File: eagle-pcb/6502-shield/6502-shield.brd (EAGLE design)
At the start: 101.6 x 53.3 mm, 45 parts, among them SW1 MCSLPT4644B1TR-TACT-SW, SW2 PCM12SMTR-SPDT-RIGHT-ANG, SW3 MCSLPT4644B1TR-TACT-SW, U1 AT28C256TSOP-28, U2 W65C02S, U3 AS6C62256, U4 W65C22, U5 MACHXO-FPGA100TQFP

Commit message: fully routed, getting close
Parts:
- removed D10, D8, D9: ACDC02-41SGWA-DUAL-7SEG, 6502-shield:ACDC02-41S-DUAL-7SEG
- removed R10, R11, R12, R13, R14, R15, R16, R17: 330, rcl:R0402
- removed SW1: MCSLPT4644B1TR-TACT-SW, 6502-shield:MCSLPT4644B1TR-TACT-SW
- removed U$1: CRYSTAL-OSC-DIP8/4, 6502-shield:DIP8/4
- removed U1: AT28C256TSOP-28, 6502-shield:SOP55P1340X120-28N
- removed U2: W65C02S, 6502-shield:QFP80P1200X1200X160-44N
- removed U3: AS6C62256, 6502-shield:SOP55P1340X120-28N
- removed U4: W65C22, 6502-shield:QFP80P1200X1200X160-44N
- added C1, C2, C5, C6, C7: 0.1uF, rcl:C0402
- added CPU: W65C02S, 6502-shield:QFP80P1200X1200X160-44N
- added EEPROM: AT28C256TSOP-28, 6502-shield:SOP55P1340X120-28N
- added EXT_XO: CRYSTAL-OSC-DIP8/4, 6502-shield:DIP8/4
- added PB_RESET: MCSLPT4644B1TR-TACT-SW, 6502-shield:MCSLPT4644B1TR-TACT-SW
- added PIO: W65C22, 6502-shield:QFP80P1200X1200X160-44N
- added RAM: AS6C62256, 6502-shield:SOP55P1340X120-28N
- D1, D2, D3, D4, D5, D6, D7: value (none) -> RED
- moved R18 40.3 mm to (68.9, 8.25), turned to 270 degrees
- moved JP2 35.0 mm to (77.3, 46.3), turned to 180 degrees
- moved C4 27.6 mm to (2.90, 30.1), turned to 180 degrees
- moved JP3 18.8 mm to (78.7, 8.40), turned to 0 degrees
- moved R1 16.8 mm to (20.0, 14.7), turned to 270 degrees
- moved D4 11.9 mm to (10.0, 43.4), turned to 180 degrees
- moved R3 11.3 mm to (12.3, 13.2), turned to 90 degrees
- moved D3 10.1 mm to (10.1, 45.0), turned to 180 degrees
- moved R19 9.32 mm to (72.5, 6.70), turned to 180 degrees
- moved D2 8.73 mm to (10.1, 46.5), turned to 180 degrees
- moved R2 8.51 mm to (15.3, 47.0)
- moved D5 7.74 mm to (20.4, 48.2), turned to 0 degrees
- moved D1 7.67 mm to (10.1, 48.0), turned to 180 degrees
- moved D6 5.72 mm to (20.4, 46.6), turned to 0 degrees
- moved R7 5.01 mm to (15.3, 45.9), turned to 180 degrees
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- renumbered SJ1 to J1, SW2 to SW_RUNHALT, SW3 to PB_STEP, U5 to FPGA
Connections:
- removed net DIGIT1_EN: D8.18, D8.3, FPGA.87
- removed net DIGIT2_EN: D8.13, D8.8, FPGA.89
- removed net DIGIT3_EN: D9.18, D9.3, FPGA.91
- removed net DIGIT4_EN: D9.13, D9.8, FPGA.94
- removed net DIGIT5_EN: D10.18, D10.3, FPGA.95
- removed net DIGIT6_EN: D10.13, D10.8, FPGA.96
- removed net DIGIT_A: FPGA.78, R10.2
- removed net DIGIT_B: FPGA.79, R11.2
- removed net DIGIT_C: FPGA.80, R12.2
- removed net DIGIT_D: FPGA.81, R13.2
- removed net DIGIT_DP: FPGA.86, R17.2
- removed net DIGIT_E: FPGA.82, R14.2
- removed net DIGIT_F: FPGA.83, R15.2
- removed net DIGIT_G: FPGA.85, R16.2
- removed net N$23: D10.12, D10.17, D8.12, D8.17, D9.12, D9.17, R10.1
- removed net N$24: D10.11, D10.16, D8.11, D8.16, D9.11, D9.16, R11.1
- removed net N$25: D10.4, D10.9, D8.4, D8.9, D9.4, D9.9, R12.1
- removed net N$26: D10.2, D10.7, D8.2, D8.7, D9.2, D9.7, R13.1
- removed net N$27: D10.1, D10.6, D8.1, D8.6, D9.1, D9.6, R14.1
- removed net N$28: D10.14, D10.19, D8.14, D8.19, D9.14, D9.19, R15.1
- removed net N$29: D10.15, D10.20, D8.15, D8.20, D9.15, D9.20, R16.1
- removed net N$30: D10.10, D10.5, D8.10, D8.5, D9.10, D9.5, R17.1
- removed net ROM_PGM: FPGA.34, PCB1.45
- new net EEPROM_PGM: FPGA.34, PCB1.23
- net A0: now also CPU.4, EEPROM.17, PCB1.44, PIO.36, RAM.17; no longer PCB1.22, U1.17, U2.4, U3.17, U4.36
- net A1: now also CPU.5, EEPROM.16, PCB1.45, PIO.35, RAM.16; no longer PCB1.24, U1.16, U2.5, U3.16, U4.35
- net A10: now also CPU.15, EEPROM.28, PCB1.34, RAM.28; no longer PCB1.42, U1.28, U2.15, U3.28
- net A11: now also CPU.16, EEPROM.2, PCB1.35, RAM.2; no longer PCB1.44, U1.2, U2.16, U3.2
- net A12: now also CPU.19, EEPROM.9, PCB1.32, RAM.9; no longer PCB1.46, U1.9, U2.19, U3.9
- net A13: now also CPU.20, EEPROM.5, PCB1.33, RAM.5; no longer PCB1.48, U1.5, U2.20, U3.5
- net A14: now also CPU.21, EEPROM.8, PCB1.30, RAM.8; no longer PCB1.50, U1.8, U2.21, U3.8
- net A15: now also CPU.22, PCB1.31; no longer PCB1.52, U2.22
- net A2: now also CPU.7, EEPROM.15, PCB1.42, PIO.34, RAM.15; no longer PCB1.26, U1.15, U2.7, U3.15, U4.34
- net A3: now also CPU.8, EEPROM.14, PCB1.43, PIO.33, RAM.14; no longer PCB1.28, U1.14, U2.8, U3.14, U4.33
- net A4: now also CPU.9, EEPROM.13, PCB1.40, RAM.13; no longer PCB1.30, U1.13, U2.9, U3.13
- net A5: now also CPU.10, EEPROM.12, PCB1.41, RAM.12; no longer PCB1.32, U1.12, U2.10, U3.12
- net A6: now also CPU.11, EEPROM.11, PCB1.38, RAM.11; no longer PCB1.34, U1.11, U2.11, U3.11
- net A7: now also CPU.12, EEPROM.10, PCB1.39, RAM.10; no longer PCB1.36, U1.10, U2.12, U3.10
- net A8: now also CPU.13, EEPROM.4, PCB1.36, RAM.4; no longer PCB1.38, U1.4, U2.13, U3.4
- net A9: now also CPU.14, EEPROM.3, PCB1.37, RAM.3; no longer PCB1.40, U1.3, U2.14, U3.3
- net BE: now also CPU.34; no longer U2.34
- net CLK: now also CPU.35, PCB1.27, PIO.21; no longer PCB1.43, U2.35, U4.21
- net D0: now also CPU.30, EEPROM.18, PCB1.52, PIO.30, RAM.18; no longer PCB1.23, U1.18, U2.30, U3.18, U4.30
- net D1: now also CPU.29, EEPROM.19, PCB1.53, PIO.29, RAM.19; no longer PCB1.25, U1.19, U2.29, U3.19, U4.29
- net D2: now also CPU.28, EEPROM.20, PCB1.50, PIO.28, RAM.20; no longer PCB1.27, U1.20, U2.28, U3.20, U4.28
- net D3: now also CPU.27, EEPROM.22, PCB1.51, PIO.26, RAM.22; no longer PCB1.29, U1.22, U2.27, U3.22, U4.26
- net D4: now also CPU.26, EEPROM.23, PCB1.48, PIO.25, RAM.23; no longer PCB1.31, U1.23, U2.26, U3.23, U4.25
- net D5: now also CPU.25, EEPROM.24, PCB1.49, PIO.24, RAM.24; no longer PCB1.33, U1.24, U2.25, U3.24, U4.24
- net D6: now also CPU.24, EEPROM.25, PCB1.46, PIO.23, RAM.25; no longer PCB1.35, U1.25, U2.24, U3.25, U4.23
- net D7: now also CPU.23, EEPROM.26, PCB1.47, PIO.22, RAM.26; no longer PCB1.37, U1.26, U2.23, U3.26, U4.22
- net DMA: now also PCB1.22; no longer PCB1.47
- net GND: now also C1.2, C2.2, C5.2, C6.2, C7.2, EEPROM.21, EXT_XO.4, PB_RESET.T2, PIO.39, RAM.21; no longer SW1.T2, U$1.4, U1.21, U3.21, U4.39
- net IO_EN: now also PIO.19; no longer U4.19
- net IRQN: now also CPU.43, PIO.17; no longer U2.43, U4.17
- net N$3: now also PB_RESET.T4; no longer SW1.T4
- net N$31: now also CPU.41; no longer U2.41
- net N$34: now also EXT_XO.5; no longer U$1.5
- net OE: now also EEPROM.1, PCB1.25, RAM.1; no longer PCB1.39, U1.1, U3.1
- net PA0: now also PIO.40; no longer U4.40
- net PA1: now also PIO.41; no longer U4.41
- net PA2: now also PIO.42; no longer U4.42
- net PA3: now also PIO.43; no longer U4.43
- net PA4: now also PIO.44; no longer U4.44
- net PA5: now also PIO.1; no longer U4.1
- net PA6: now also PIO.2; no longer U4.2
- net PA7: now also PIO.3; no longer U4.3
- net PB0: now also PIO.4; no longer U4.4
- net PB1: now also PIO.6; no longer U4.6
- net PB2: now also PIO.7; no longer U4.7
- net PB3: now also PIO.8; no longer U4.8
- net PB4: now also PIO.9; no longer U4.9
- net PB5: now also PIO.10; no longer U4.10
- net PB6: now also PIO.11; no longer U4.11
- net PB7: now also PIO.12; no longer U4.12
- net RAM_EN: now also RAM.27; no longer U3.27
- net RESETN: now also CPU.38, PIO.31; no longer U2.38, U4.31
- net ROM_EN: now also EEPROM.27; no longer U1.27
- net RW: now also CPU.32, PIO.18; no longer U2.32, U4.18
- net VCC: now also C1.1, C2.1, C5.1, C6.1, C7.1, CPU.1, CPU.3, CPU.31, EEPROM.7, EXT_XO.8, PIO.15, PIO.20, RAM.7; no longer U$1.8, U1.7, U2.1, U2.3, U2.31, U3.7, U4.15, U4.20
- net WE: now also EEPROM.6, PCB1.29, RAM.6; no longer PCB1.41, U1.6, U3.6
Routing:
- net VCC: track 0.00 -> 368.6 mm, vias 0 -> 8
- net IRQN: track 0.00 -> 178.4 mm, vias 0 -> 4
- net CLK: track 0.00 -> 159.1 mm, vias 0 -> 4
- net EEPROM_PGM: track 0.00 -> 153.0 mm, vias 0 -> 2
- net DMA: track 0.00 -> 137.7 mm, vias 0 -> 2
- net RW: track 0.00 -> 132.3 mm, vias 0 -> 3
- net A10: track 0.00 -> 123.9 mm, vias 0 -> 4
- net D0: track 0.00 -> 123.1 mm, vias 0 -> 5
- net D1: track 0.00 -> 118.4 mm, vias 0 -> 5
- net A13: track 0.00 -> 117.3 mm, vias 0 -> 4
- net WE: track 0.00 -> 114.5 mm, vias 0 -> 3
- net D2: track 0.00 -> 112.4 mm, vias 0 -> 5
- net A3: track 0.00 -> 111.1 mm, vias 0 -> 5
- net A14: track 0.00 -> 108.8 mm, vias 0 -> 4
- net A15: track 0.00 -> 108.2 mm, vias 0 -> 2
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- added copper zone on layer 1, net GND
- added copper zone on layer 16, net GND
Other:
- board text added: "6502-shield REV A"
- board text added: "CLK"
- board text added: "CLOCK SELECT"
- board text added: "FPGA"
- board text added: "FPGA JTAG"
- board text added: "GND"
- board text added: "HALT"
- board text added: "IRQ"
- board text added: "LCD"
- board text added: "OPTIONAL 3.3VDC XO"
- board text added: "PA7"
- board text added: "PB7"
- board text added: "PIO"
- board text added: "R/W"
- board text added: "RAM"
- board text added: "RESET"
- board text added: "ROM"
- board text added: "RUN"
- board text added: "STEP"
- board text added: "TCK"
- board text added: "TDI"
- board text added: "TDO"
- board text added: "TMS"
- board text added: "VCC"
- board text added: "XO"
- board text added: "github.com/impavidus"

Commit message: This should be ready to send out.
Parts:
- EEPROM: value AT28C256TSOP-28 -> AT28BV256TSOP-28
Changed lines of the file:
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@@
 <layer number="201" name="201bmp" color="2" fill="1" visible="no" active="no"/>
 <layer number="202" name="202bmp" color="3" fill="1" visible="no" active="no"/>
+<layer number="203" name="203bmp" color="4" fill="10" visible="no" active="yes"/>
+<layer number="204" name="204bmp" color="5" fill="10" visible="no" active="yes"/>
+<layer number="205" name="205bmp" color="6" fill="10" visible="no" active="yes"/>
+<layer number="206" name="206bmp" color="7" fill="10" visible="no" active="yes"/>
+<layer number="207" name="207bmp" color="8" fill="10" visible="no" active="yes"/>
+<layer number="208" name="208bmp" color="9" fill="10" visible="no" active="yes"/>
+<layer number="209" name="209bmp" color="7" fill="1" visible="no" active="yes"/>
+<layer number="210" name="210bmp" color="7" fill="1" visible="no" active="yes"/>
+<layer number="211" name="211bmp" color="7" fill="1" visible="no" active="yes"/>
+<layer number="212" name="212bmp" color="7" fill="1" visible="no" active="yes"/>
+<layer number="213" name="213bmp" color="7" fill="1" visible="no" active="yes"/>
+<layer number="214" name="214bmp" color="7" fill="1" visible="no" active="yes"/>
+<layer number="215" name="215bmp" color="7" fill="1" visible="no" active="yes"/>
+<layer number="216" name="216bmp" color="7" fill="1" visible="no" active="yes"/>
 <layer number="217" name="217bmp" color="18" fill="1" visible="no" active="no"/>
 <layer number="218" name="218bmp" color="19" fill="1" visible="no" active="no"/>
@@
 <layer number="223" name="223bmp" color="24" fill="1" visible="no" active="no"/>
 <layer number="224" name="224bmp" color="25" fill="1" visible="no" active="no"/>
+<layer number="225" name="225bmp" color="7" fill="1" visible="yes" active="yes"/>
+<layer number="226" name="226bmp" color="7" fill="1" visible="yes" active="yes"/>
+<layer number="227" name="227bmp" color="7" fill="1" visible="yes" active="yes"/>
+<layer number="228" name="228bmp" color="7" fill="1" visible="yes" active="yes"/>
+<layer number="229" name="229bmp" color="7" fill="1" visible="yes" active="yes"/>
+<layer number="230" name="230bmp" color="7" fill="1" visible="yes" active="yes"/>
 <layer number="231" name="Eagle3D_PG1" color="7" fill="1" visible="no" active="no"/>
 <layer number="232" name="Eagle3D_PG2" color="7" fill="1" visible="no" active="no"/>
 <layer number="233" name="Eagle3D_PG3" color="7" fill="1" visible="no" active="no"/>
+<layer number="248" name="Housing" color="7" fill="1" visible="no" active="yes"/>
+<layer number="249" name="Edge" color="7" fill="1" visible="no" active="yes"/>
 <layer number="250" name="Descript" color="7" fill="1" visible="no" active="no"/>
 <layer number="251" name="SMDround" color="7" fill="1" visible="no" active="no"/>
+<layer number="254" name="cooling" color="7" fill="1" visible="no" active="yes"/>
+<layer number="255" name="routoute" color="7" fill="1" visible="yes" active="yes"/>
 </layers>
 <board>
-<fusionsync huburn="a.YnVzaW5lc3M6Z21haWw3MDQ2MzI" projecturn="a.YnVzaW5lc3M6Z21haWw3MDQ2MzIjMjAyMDAzMjMyNzc5NDAzNTE" f3durn="urn:adsk.wipprod:dm.lineage:SKI6Y7I3R2GK5LyZdhPrew" pcbguid="6684de3e-4798-432d-a463-1731bf560a7c" lastpulledtime="2020-03-23T21:54:50Z" lastsyncedchangeguid="26928c01-5e82-ac68-2b74-82bd82c14e25" latestrevisionid="" lastsyncedrevisionid="" lastboardhashguid="0d8e985b-e84f-ecb9-3e28-55cf7d987780" lastpushedtime="2020-04-09T22:58:09Z" linktopcb3d="%12"/>
+<fusionsync huburn="a.YnVzaW5lc3M6Z21haWw3MDQ2MzI" projecturn="a.YnVzaW5lc3M6Z21haWw3MDQ2MzIjMjAyMDAzMjMyNzc5NDAzNTE" f3durn="urn:adsk.wipprod:dm.lineage:SKI6Y7I3R2GK5LyZdhPrew" pcbguid="6684de3e-4798-432d-a463-1731bf560a7c" lastpulledtime="2020-03-23T21:54:50Z" lastsyncedchangeguid="26928c01-5e82-ac68-2b74-82bd82c14e25" latestrevisionid="" lastsyncedrevisionid="" lastboardhashguid="5e5b8b2a-9c23-a083-ff8b-f57618442608" lastpushedtime="2020-04-10T03:47:32Z" linktopcb3d="%12"/>
 <plain>
 <text x="1.5" y="43.5" size="0.8128" layer="21" font="vector" ratio="15" rot="R90">RUN</text>
@@
 <text x="76.4" y="10.6" size="1.016" layer="21" font="vector" ratio="15" rot="R90">VCC</text>
 <text x="81.5" y="10.6" size="1.016" layer="21" font="vector" ratio="15" rot="R90">GND</text>
-<text x="30.05" y="41.95" size="2.54" layer="21">github.com/impavidus</text>
-<text x="2.9" y="0.7" size="0.8128" layer="21" rot="R90">6502-shield
+<text x="29.1" y="43.45" size="2.54" layer="21">github.com/impavidus</text>
+<text x="10.885703125" y="49.590428125" size="1.016" layer="22" font="vector" ratio="15" rot="MR0">6502-shield
+REV A</text>
+<text x="10.885703125" y="49.590428125" size="1.016" layer="22" font="vector" ratio="15" rot="MR0">6502-shield
 REV A</text>
 </plain>
@@
 </autorouter>
 <elements>
-<element name="PCB1" library="E14_Arduino_revC" library_urn="urn:adsk.eagle:library:18477430" package="ARDUINO_MEGA2560" package3d_urn="urn:adsk.eagle:package:18477461/4" value="ARDUINO_MEGA2560" x="0" y="0" locked="yes" smashed="yes"/>
+<element name="PCB1" library="E14_Arduino_revC" library_urn="urn:adsk.eagle:library:18477430" package="ARDUINO_MEGA2560" package3d_urn="urn:adsk.eagle:package:18477461/5" value="ARDUINO_MEGA2560" x="0" y="0" locked="yes" smashed="yes"/>
 <element name="PB_RESET" library="6502-shield" library_urn="urn:adsk.eagle:library:18477216" package="MCSLPT4644B1TR-TACT-SW" package3d_urn="urn:adsk.eagle:package:18592201/6" value="MCSLPT4644B1TR-TACT-SW" x="7.83" y="4.76" smashed="yes" rot="R180">
 <attribute name="VALUE" x="11.13" y="8.66" size="1.27" layer="27" rot="R180"/>
@@
 <attribute name="VALUE" x="3.535" y="31.985" size="1.27" layer="27" rot="R180"/>
 </element>
-<element name="EEPROM" library="6502-shield" library_urn="urn:adsk.eagle:library:18477216" package="SOP55P1340X120-28N" package3d_urn="urn:adsk.eagle:package:18436546/2" value="AT28C256TSOP-28" x="47.28" y="26.8" smashed="yes" rot="R270">
+<element name="EEPROM" library="6502-shield" library_urn="urn:adsk.eagle:library:18477216" package="SOP55P1340X120-28N" package3d_urn="urn:adsk.eagle:package:18436546/2" value="AT28BV256TSOP-28" x="47.28" y="26.8" smashed="yes" rot="R270">
 <attribute name="NAME" x="40.884" y="26.75" size="1.27" layer="25" rot="R270" align="bottom-center"/>
 <attribute name="VALUE" x="42.595" y="26.8" size="1.27" layer="27" rot="R270" align="top-center"/>
@@
 </signals>
 <mfgpreviewcolors>
-<mfgpreviewcolor name="soldermaskcolor" color="0xC8800080"/>
+<mfgpreviewcolor name="soldermaskcolor" color="0xC86D0A8E"/>
 <mfgpreviewcolor name="silkscreencolor" color="0xFFFFFFFF"/>
 <mfgpreviewcolor name="backgroundcolor" color="0xFF282828"/>

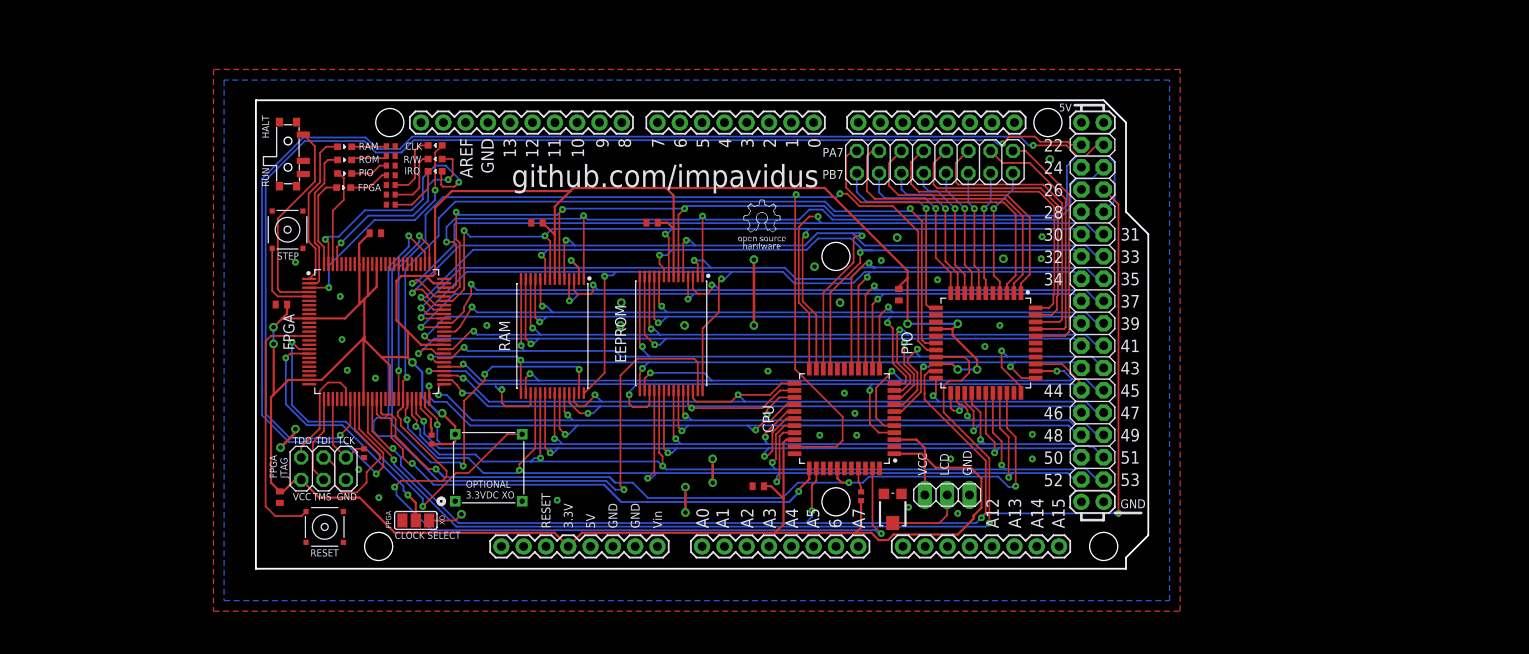
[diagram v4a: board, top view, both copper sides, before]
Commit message: Fixed problems with FPGA pinout in component library, updated schematic and cleaned it up a bunch.  Fixed external clock not coming into FPGA on dedicated clock net pin. More schematic work on the list still.
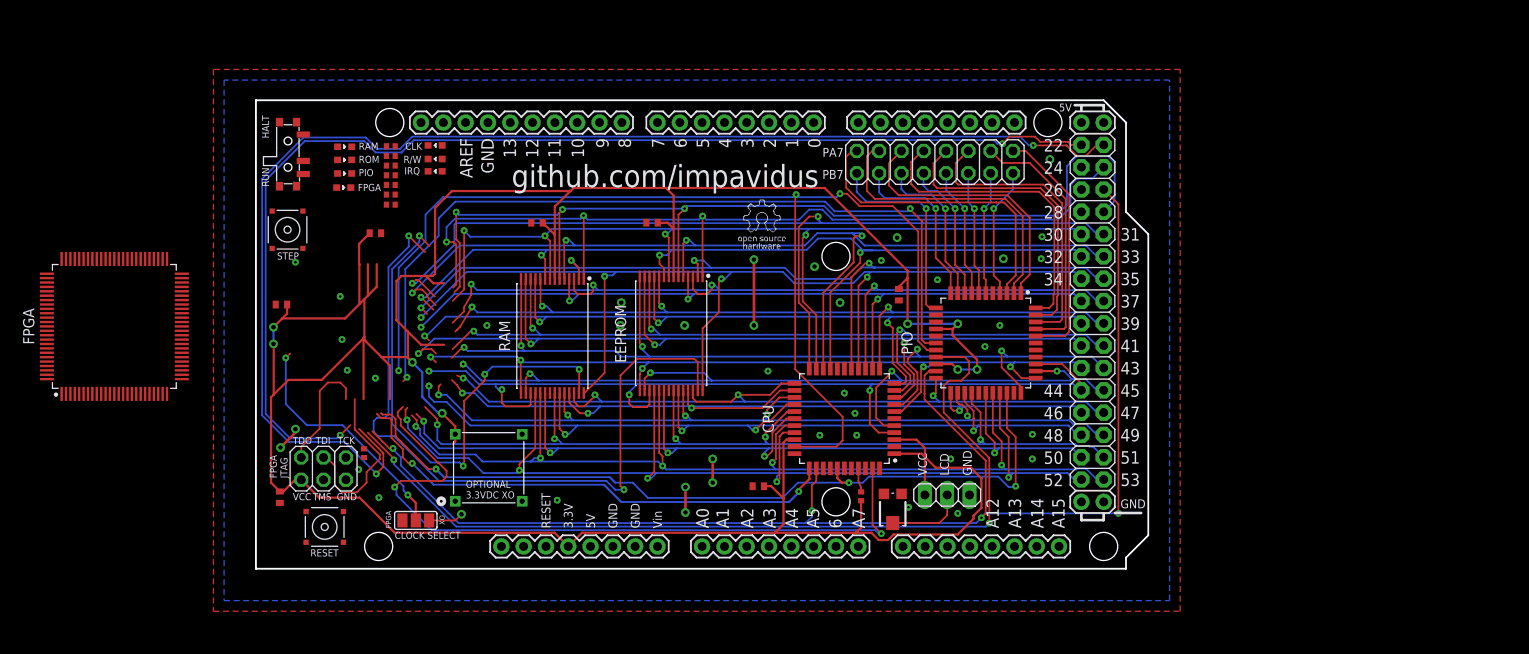
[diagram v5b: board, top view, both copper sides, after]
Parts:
- removed R1: 10K, rcl:R0402
- FPGA: value MACHXO-FPGA100TQFP -> MACHXO2-FPGA100TQFP
- moved FPGA 29.9 mm to (-16.1, 27.6), turned to 90 degrees
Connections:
- removed net N$1: FPGA.48, R1.1
- removed net N$16: D4.2, FPGA.100
- removed net N$17: D7.2, FPGA.99
- removed net N$18: D3.2, FPGA.98
- removed net N$19: D6.2, FPGA.97
- removed net N$2: FPGA.5, PB_STEP.T4
- removed net N$20: D1.1, R4.1
- removed net N$21: D2.1, R2.1
- removed net N$22: D5.1, R5.1
- removed net N$3: FPGA.14, PB_RESET.T4
- removed net N$34: EXT_XO.5, FPGA.17
- removed net N$4: FPGA.31, JP1.2
- removed net N$5: FPGA.26, JP1.3
- removed net N$6: FPGA.33, JP1.4
- removed net N$7: FPGA.28, JP1.6, R3.2
- removed net N$8: FPGA.4, SW_RUNHALT.1
- new net EXT_CLK: EXT_XO.5, FPGA.88
- new net LED_0: FPGA.76, R5.2
- new net LED_1: FPGA.77, R6.2
- new net LED_2: FPGA.81, R7.2
- new net LED_3: FPGA.82, R8.2
- new net LED_4: FPGA.85, R9.2
- new net LED_5: FPGA.86, R4.2
- new net LED_6: FPGA.87, R2.2
- new net PB_RESET: FPGA.3, PB_RESET.T3
- new net PB_STEP: FPGA.2, PB_STEP.T3
- new net SW_RUNHALT: FPGA.1, SW_RUNHALT.1
- new net TCK: FPGA.91, JP1.6, R3.2
- new net TDI: FPGA.94, JP1.4
- new net TDO: FPGA.95, JP1.2
- new net TMS: FPGA.90, JP1.3
- net A0: now also FPGA.38; no longer FPGA.54
- net A1: now also FPGA.39; no longer FPGA.55
- net A10: now also FPGA.53; no longer FPGA.66
- net A11: now also FPGA.54; no longer FPGA.67
- net A12: now also FPGA.57; no longer FPGA.68
- net A13: now also FPGA.58; no longer FPGA.69
- net A14: now also FPGA.62; no longer FPGA.70
- net A15: now also FPGA.63; no longer FPGA.71
- net A2: now also FPGA.40; no longer FPGA.56
- net A3: now also FPGA.41; no longer FPGA.57
- net A4: now also FPGA.42; no longer FPGA.58
- net A5: now also FPGA.43; no longer FPGA.59
- net A6: now also FPGA.48; no longer FPGA.61
- net A7: now also FPGA.49; no longer FPGA.63
- net A8: now also FPGA.51; no longer FPGA.64
- net A9: now also FPGA.52; no longer FPGA.65
- net BE: now also FPGA.13; no longer FPGA.38
- net CLK: now also FPGA.12; no longer FPGA.37
- net CLK_SEL: now also FPGA.99; no longer FPGA.18
- net D0: now also FPGA.24; no longer FPGA.45
- net D1: now also FPGA.25; no longer FPGA.46
- net D2: now also FPGA.27; no longer FPGA.47
- net D3: now also FPGA.28; no longer FPGA.49
- net D4: now also FPGA.31; no longer FPGA.50
- net D5: now also FPGA.32; no longer FPGA.51
- net D6: now also FPGA.34; no longer FPGA.52
- net D7: now also FPGA.35; no longer FPGA.53
- net DMA: now also FPGA.74; no longer FPGA.32
- net EEPROM_PGM: now also FPGA.75; no longer FPGA.34
- net GND: now also D1.1, D2.1, D3.1, D4.1, D5.1, D6.1, D7.1, FPGA.22, FPGA.33, FPGA.44, FPGA.56, FPGA.6, FPGA.72, FPGA.79, FPGA.92; no longer FPGA.12, FPGA.25, FPGA.40, FPGA.42, FPGA.62, FPGA.75, FPGA.84, FPGA.93, R2.2, R4.2, R5.2, R6.1, R7.1, R8.1, R9.1
- net IO_EN: now also FPGA.16; no longer FPGA.36
- net IRQN: now also FPGA.70; no longer FPGA.44
- net N$10: now also R6.1; no longer FPGA.2
- net N$11: now also R7.1; no longer FPGA.3
- net N$12: now also D4.2, R8.1; no longer D6.1, R6.2
- net N$13: now also D3.2, R9.1; no longer D3.1, R7.2
- net N$14: now also D6.2, R4.1; no longer D7.1, R8.2
- net N$15: now also D7.2, R2.1; no longer D4.1, R9.2
- net N$9: now also R5.1; no longer FPGA.1
- net OE: now also FPGA.66; no longer FPGA.73
- net RAM_EN: now also FPGA.17; no longer FPGA.76
- net RESETN: now also FPGA.21; no longer FPGA.39
- net ROM_EN: now also FPGA.20; no longer FPGA.77
- net RW: now also FPGA.71; no longer FPGA.43
- net VCC: now also FPGA.100, FPGA.23, FPGA.26, FPGA.46, FPGA.5, FPGA.50, FPGA.55, FPGA.73, FPGA.80, FPGA.93; no longer FPGA.10, FPGA.24, FPGA.35, FPGA.41, FPGA.60, FPGA.74, FPGA.88, FPGA.90, FPGA.92, R1.2
- net WE: now also FPGA.67; no longer FPGA.72
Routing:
- net N$34: track 44.4 -> 0.00 mm, vias 2 -> 0
- net N$3: track 29.3 -> 0.00 mm
- net N$17: track 28.0 -> 0.00 mm, vias 2 -> 0
- net N$11: track 26.5 -> 0.00 mm, vias 2 -> 0
- net N$8: track 23.6 -> 0.00 mm
- net N$19: track 22.5 -> 0.00 mm, vias 2 -> 0
- net TDI: track 0.00 -> 19.6 mm
- net N$6: track 19.6 -> 0.00 mm
- net N$9: track 17.8 -> 0.00 mm
- net N$10: track 17.0 -> 0.00 mm
- net TDO: track 0.00 -> 13.3 mm
- net N$4: track 13.3 -> 0.00 mm
- net N$18: track 11.2 -> 0.00 mm
- net N$16: track 10.6 -> 0.00 mm
- net N$5: track 10.2 -> 0.00 mm
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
